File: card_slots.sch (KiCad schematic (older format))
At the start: 0 parts

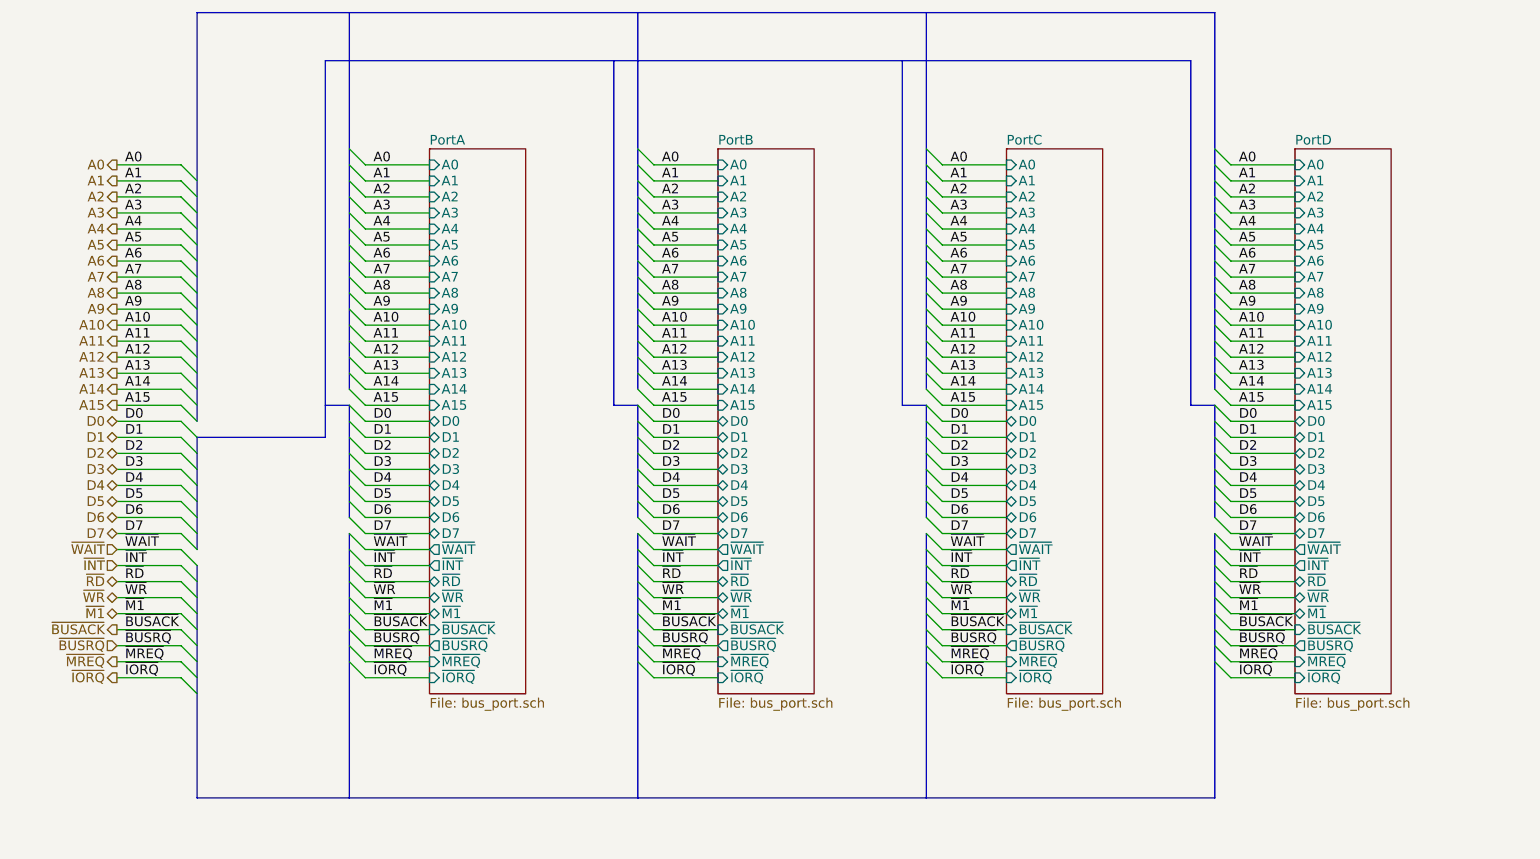
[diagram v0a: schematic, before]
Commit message: Added seperate power pin slots to stop inserting cards backwards
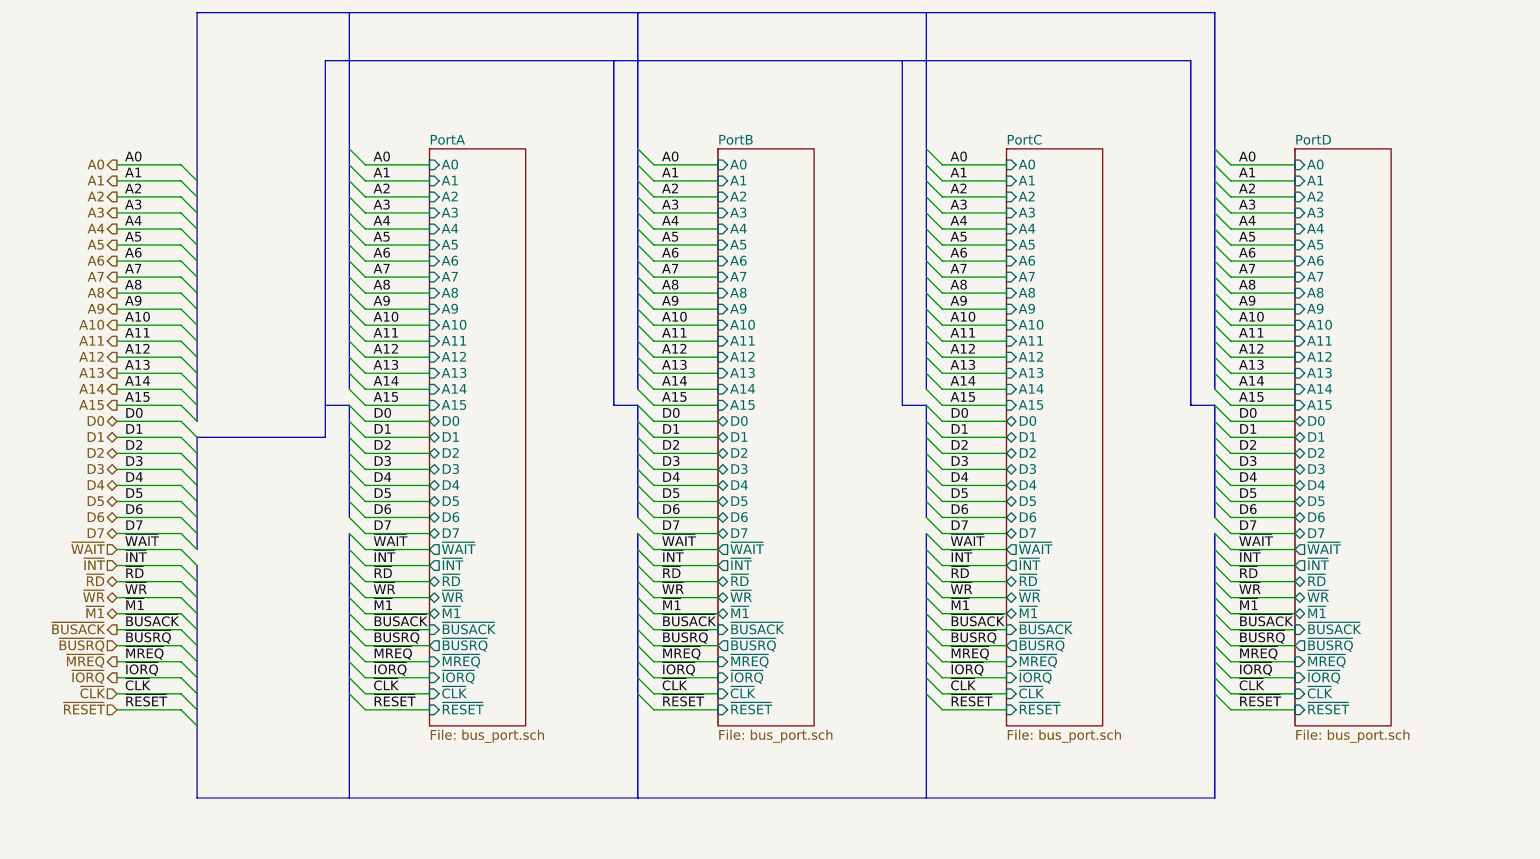
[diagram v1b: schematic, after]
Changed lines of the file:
@@
 $EndDescr
 $Sheet
-S 3650 1950 600  3400
+S 3650 1950 600  3600
 U 577F1897
 F0 "PortA" 60
@@
 F33 "~MREQ" I L 3650 5150 60
 F34 "~IORQ" I L 3650 5250 60
+F35 "~CLK" I L 3650 5350 60
+F36 "~RESET" I L 3650 5450 60
 $EndSheet
 $Sheet
-S 5450 1950 600  3400
+S 5450 1950 600  3600
 U 577F7EB3
 F0 "PortB" 60
@@
 F33 "~MREQ" I L 5450 5150 60
 F34 "~IORQ" I L 5450 5250 60
+F35 "~CLK" I L 5450 5350 60
+F36 "~RESET" I L 5450 5450 60
 $EndSheet
 $Sheet
-S 7250 1950 600  3400
+S 7250 1950 600  3600
 U 577F8AF5
 F0 "PortC" 60
@@
 F33 "~MREQ" I L 7250 5150 60
 F34 "~IORQ" I L 7250 5250 60
+F35 "~CLK" I L 7250 5350 60
+F36 "~RESET" I L 7250 5450 60
 $EndSheet
 $Sheet
-S 9050 1950 600  3400
+S 9050 1950 600  3600
 U 577F9440
 F0 "PortD" 60
@@
 F33 "~MREQ" I L 9050 5150 60
 F34 "~IORQ" I L 9050 5250 60
+F35 "~CLK" I L 9050 5350 60
+F36 "~RESET" I L 9050 5450 60
 $EndSheet
 Wire Wire Line
@@
 Wire Bus Line
 	2200 1100 2200 3650
+Text HLabel 1700 5350 0    60   Input ~ 0
+~CLK
+Wire Wire Line
+	1700 5350 2100 5350
+Entry Wire Line
+	2100 5350 2200 5450
+Text Label 1750 5350 0    60   ~ 0
+~CLK
+Wire Wire Line
+	9050 5350 8650 5350
+Entry Wire Line
+	8550 5250 8650 5350
+Text Label 8700 5350 0    60   ~ 0
+~CLK
+Wire Wire Line
+	7250 5350 6850 5350
+Entry Wire Line
+	6750 5250 6850 5350
+Text Label 6900 5350 0    60   ~ 0
+~CLK
+Wire Wire Line
+	5450 5350 5050 5350
+Entry Wire Line
+	4950 5250 5050 5350
+Text Label 5100 5350 0    60   ~ 0
+~CLK
+Wire Wire Line
+	3650 5350 3250 5350
+Entry Wire Line
+	3150 5250 3250 5350
+Text Label 3300 5350 0    60   ~ 0
+~CLK
+Wire Wire Line
+	3650 5450 3250 5450
+Entry Wire Line
+	3150 5350 3250 5450
+Text Label 3300 5450 0    60   ~ 0
+~RESET
+Wire Wire Line
+	5450 5450 5050 5450
+Entry Wire Line
+	4950 5350 5050 5450
+Text Label 5100 5450 0    60   ~ 0
+~RESET
+Wire Wire Line
+	7250 5450 6850 5450
+Entry Wire Line
+	6750 5350 6850 5450
+Text Label 6900 5450 0    60   ~ 0
+~RESET
+Wire Wire Line
+	9050 5450 8650 5450
+Entry Wire Line
+	8550 5350 8650 5450
+Text Label 8700 5450 0    60   ~ 0
+~RESET
+Text HLabel 1700 5450 0    60   Input ~ 0
+~RESET
+Wire Wire Line
+	1700 5450 2100 5450
+Entry Wire Line
+	2100 5450 2200 5550
+Text Label 1750 5450 0    60   ~ 0
+~RESET
 $EndSCHEMATC

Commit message: More card slot clean up. Added NMI signal for DMA
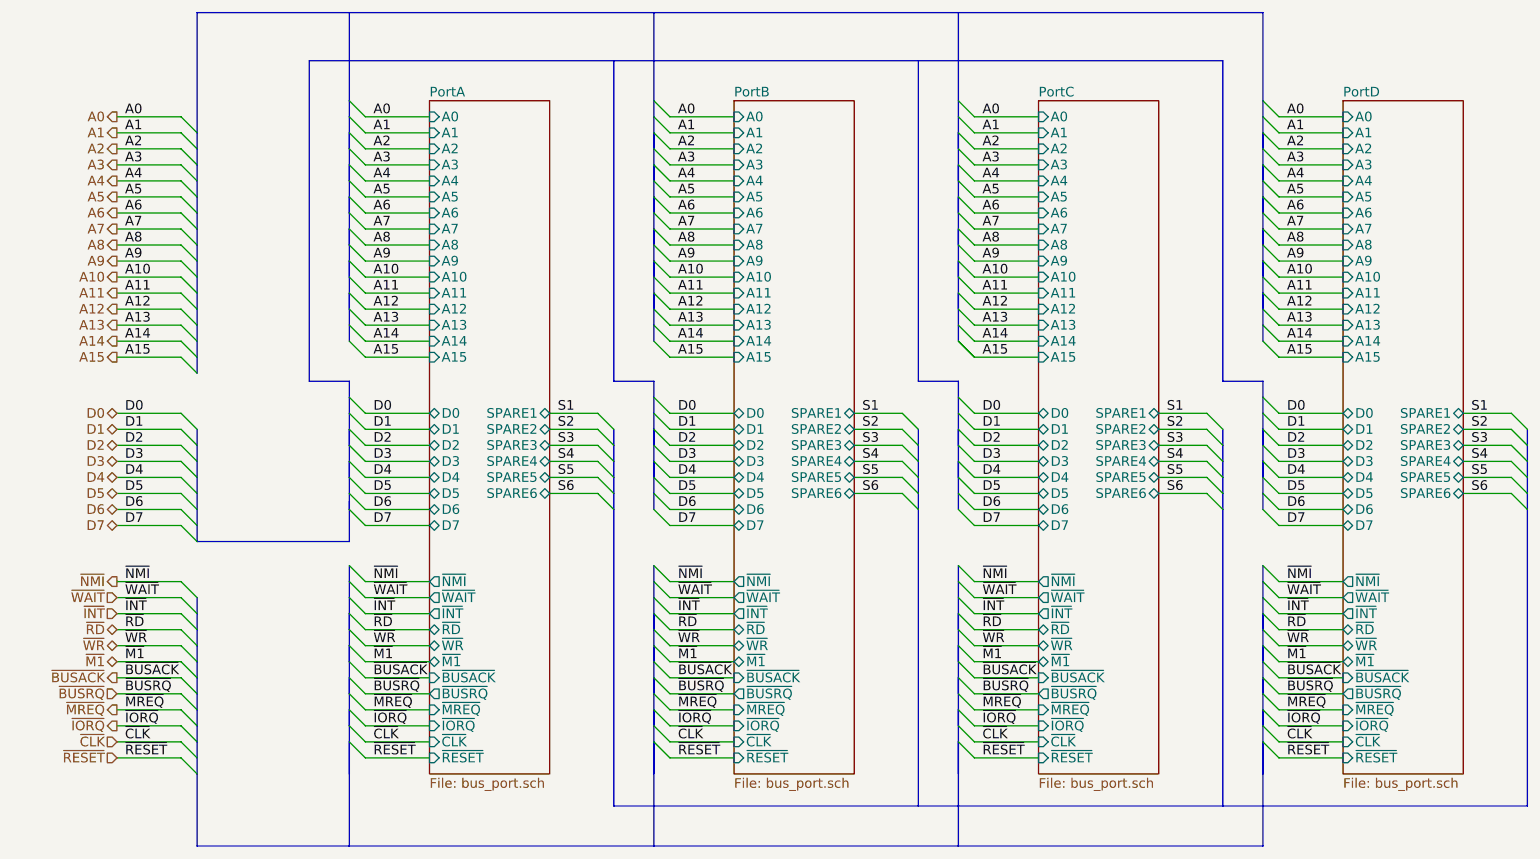
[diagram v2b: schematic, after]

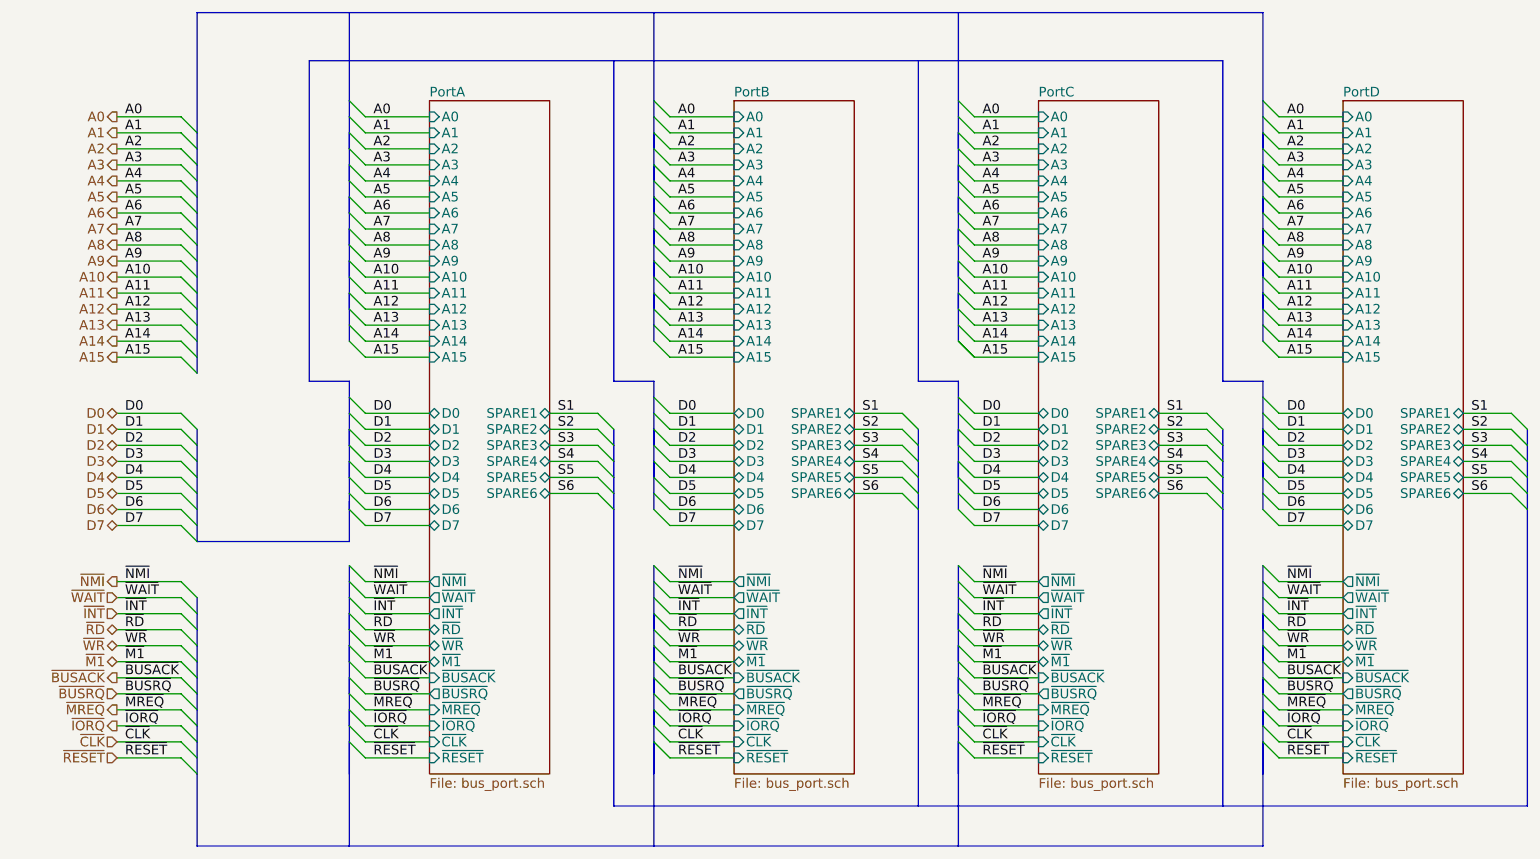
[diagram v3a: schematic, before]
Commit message: Added IO address decoder, 8 IO slots, partial IO bus buffering. Still to decide: what to do with all the /INT pins? TODO: add bi-directional data bus buffering (2x 74AC241?) for IO boards. This thing is turning into a monster :)
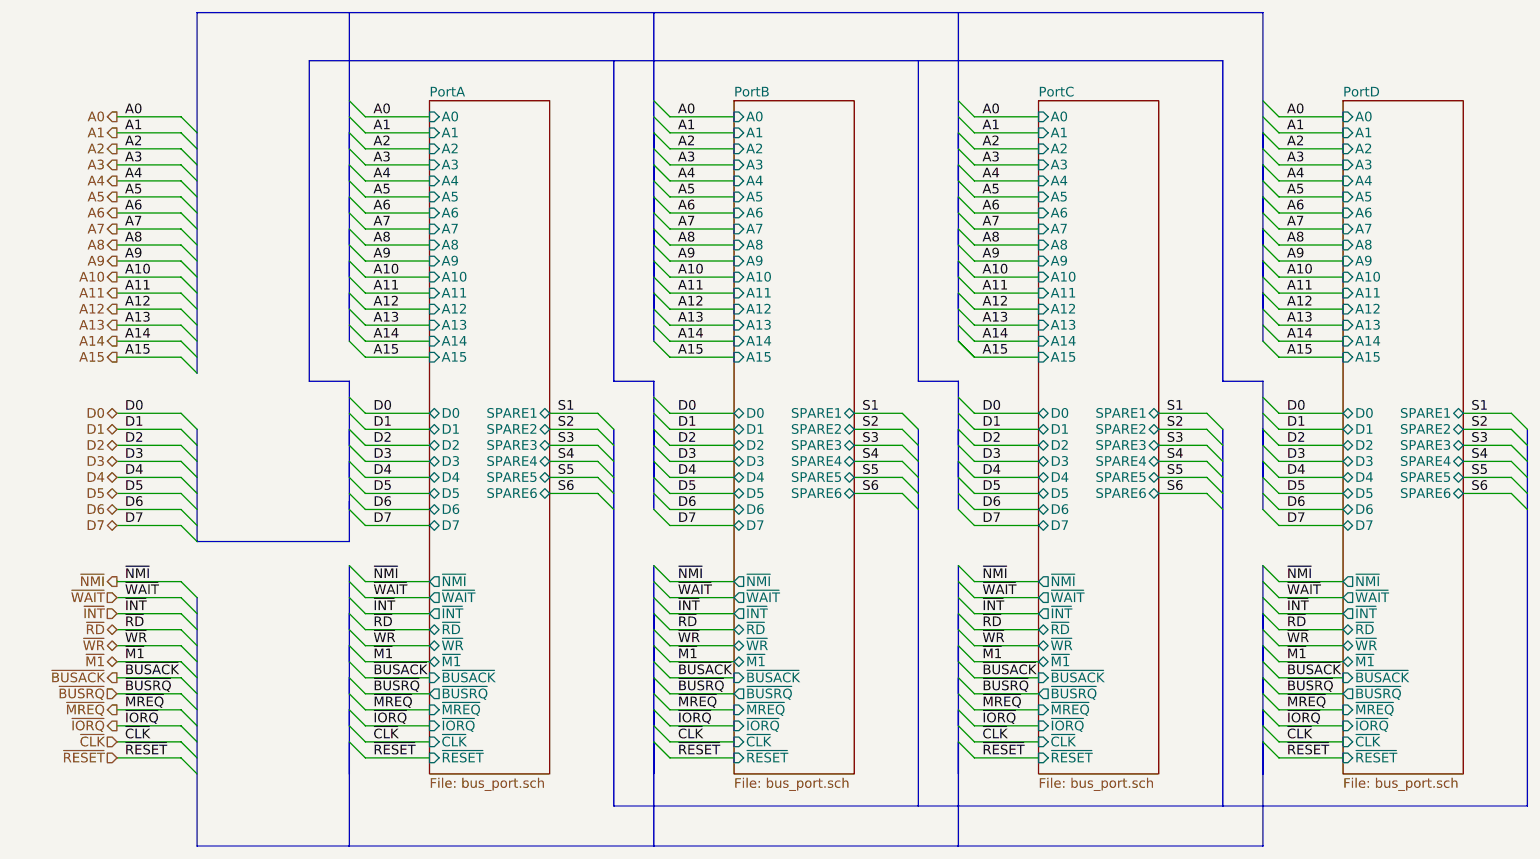
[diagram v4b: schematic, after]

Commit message: Added missing signals to IO and added buffer
I've removed the /WAIT and also added a somewhat dodgy diode AND to
handle the bi-directional Dx buffer. Might work, might not.

Also cleaned up the buses and just tidied things up.
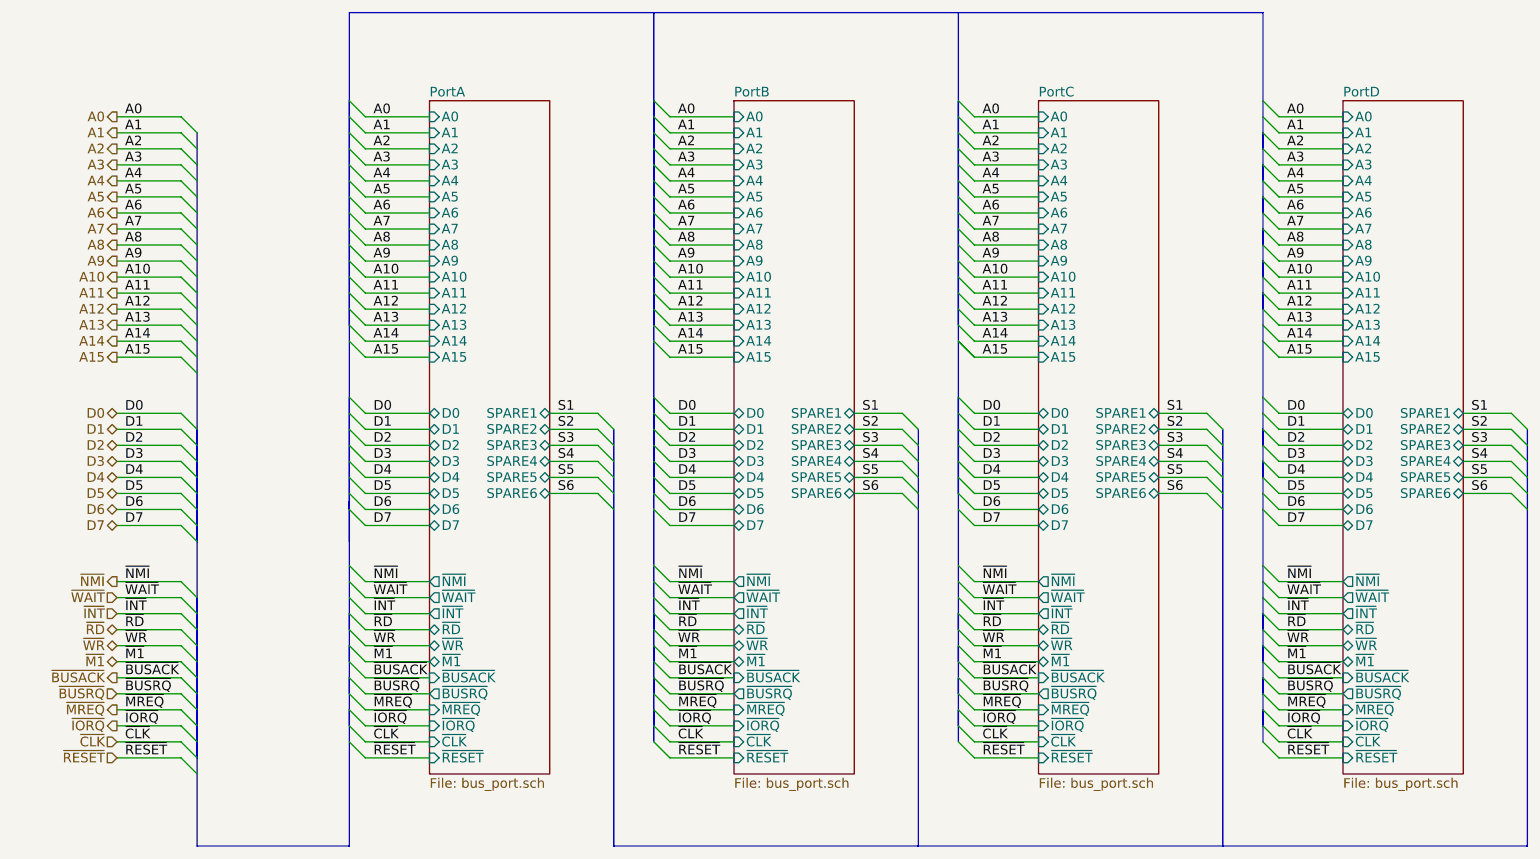
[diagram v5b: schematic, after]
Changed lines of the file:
@@
 	3650 5550 3250 5550
 Wire Bus Line
-	3150 1100 3150 3150
-Wire Bus Line
-	3150 1850 3150 1950
-Wire Bus Line
-	3150 2050 3150 2150
-Wire Bus Line
-	3150 2250 3150 2350
-Wire Bus Line
-	3150 2450 3150 2550
-Wire Bus Line
-	3150 2650 3150 2750
-Wire Bus Line
-	3150 2850 3150 2950
-Wire Bus Line
-	3150 3400 3150 4400
-Wire Bus Line
-	3150 3700 3150 3800
-Wire Bus Line
-	3150 3900 3150 4000
-Wire Bus Line
-	3150 4550 3150 5850
+	3150 1100 3150 4400
+Wire Bus Line
+	3150 1650 3150 3050
+Wire Bus Line
+	3150 3500 3150 6300
 Wire Bus Line
 	3150 4850 3150 4950
@@
 Wire Bus Line
 	3150 5450 3150 5550
-Wire Bus Line
-	3150 5650 3150 6300
 Wire Wire Line
 	2100 1750 1700 1750
@@
 	2100 5550 1700 5550
 Wire Bus Line
-	2200 4750 2200 6300
+	2200 1850 2200 6300
 Wire Bus Line
 	2200 3700 2200 4400
 Wire Bus Line
-	2200 1100 2200 3350
+	2200 4750 2200 5750
 Wire Wire Line
 	1700 5650 2100 5650
@@
 Wire Wire Line
 	1700 4650 2100 4650
-Wire Bus Line
-	2200 1100 8850 1100
-Wire Bus Line
-	2200 6300 8850 6300
 Wire Wire Line
 	4400 3600 4700 3600
@@
 	4400 4100 4700 4100
 Wire Bus Line
-	4800 3700 4800 6050
+	4800 3700 4800 6300
 $Sheet
 S 5550 1650 750  4200
@@
 	5550 5550 5150 5550
 Wire Bus Line
-	5050 1100 5050 3150
-Wire Bus Line
-	5050 1850 5050 1950
-Wire Bus Line
-	5050 2050 5050 2150
-Wire Bus Line
-	5050 2250 5050 2350
-Wire Bus Line
-	5050 2450 5050 2550
-Wire Bus Line
-	5050 2650 5050 2750
-Wire Bus Line
-	5050 2850 5050 2950
-Wire Bus Line
-	5050 3400 5050 4200
-Wire Bus Line
-	5050 3700 5050 3800
-Wire Bus Line
-	5050 3900 5050 4000
-Wire Bus Line
-	5050 4550 5050 5850
+	5050 1100 5050 5650
+Wire Bus Line
+	5050 1650 5050 3050
+Wire Bus Line
+	5050 3500 5050 4100
 Wire Bus Line
 	5050 4850 5050 4950
@@
 Wire Bus Line
 	5050 5450 5050 5550
-Wire Bus Line
-	5050 5650 5050 6300
 Wire Wire Line
 	5550 5650 5150 5650
@@
 	6300 4100 6600 4100
 Wire Bus Line
-	6700 3700 6700 6050
+	6700 3700 6700 6300
 Wire Wire Line
 	4400 3900 4700 3900
@@
 	7450 5550 7050 5550
 Wire Bus Line
-	6950 1100 6950 3150
-Wire Bus Line
-	6950 1850 6950 1950
-Wire Bus Line
-	6950 2050 6950 2150
-Wire Bus Line
-	6950 2250 6950 2350
-Wire Bus Line
-	6950 2450 6950 2550
-Wire Bus Line
-	6950 2650 6950 2750
-Wire Bus Line
-	6950 2850 6950 2950
-Wire Bus Line
-	6950 3400 6950 4200
-Wire Bus Line
-	6950 3700 6950 3800
-Wire Bus Line
-	6950 3900 6950 4000
-Wire Bus Line
-	6950 4550 6950 5850
+	6950 1100 6950 5650
+Wire Bus Line
+	6950 1650 6950 3050
+Wire Bus Line
+	6950 3500 6950 4100
 Wire Bus Line
 	6950 4850 6950 4950
@@
 Wire Bus Line
 	6950 5450 6950 5550
-Wire Bus Line
-	6950 5650 6950 6300
 Wire Wire Line
 	7450 5650 7050 5650
@@
 	8200 4100 8500 4100
 Wire Bus Line
-	8600 3700 8600 6050
+	8600 3700 8600 6300
 $Sheet
 S 9350 1650 750  4200
@@
 	9350 5550 8950 5550
 Wire Bus Line
-	8850 1100 8850 3150
+	8850 1100 8850 5650
 Wire Bus Line
 	8850 1850 8850 1950
@@
 	8850 2850 8850 2950
 Wire Bus Line
-	8850 3400 8850 4200
-Wire Bus Line
 	8850 3700 8850 3800
 Wire Bus Line
 	8850 3900 8850 4000
 Wire Bus Line
-	8850 4550 8850 5850
-Wire Bus Line
 	8850 4850 8850 4950
 Wire Bus Line
@@
 Wire Bus Line
 	8850 5450 8850 5550
-Wire Bus Line
-	8850 6300 8850 5650
 Wire Wire Line
 	9350 5650 8950 5650
@@
 	10100 4100 10400 4100
 Wire Bus Line
-	10500 3700 10500 6050
-Wire Bus Line
-	4800 1400 4800 3400
-Wire Bus Line
-	4800 3400 5050 3400
+	10500 3700 10500 6300
 Entry Wire Line
 	6950 3150 7050 3250
 Wire Bus Line
-	6700 1400 6700 3400
-Wire Bus Line
-	6700 3400 6950 3400
-Wire Bus Line
-	8600 1400 8600 3400
-Wire Bus Line
-	8600 3400 8850 3400
-Wire Bus Line
-	10500 6050 4800 6050
-Wire Bus Line
-	2900 1400 2900 3400
-Wire Bus Line
-	2900 3400 3150 3400
-Wire Bus Line
-	2900 1400 8600 1400
-Wire Bus Line
-	2200 4400 3150 4400
+	10500 6300 4800 6300
 Wire Bus Line
 	3150 4200 3150 4150
+Wire Bus Line
+	3150 1100 8850 1100
+Wire Bus Line
+	2200 6300 3150 6300
 $EndSCHEMATC
